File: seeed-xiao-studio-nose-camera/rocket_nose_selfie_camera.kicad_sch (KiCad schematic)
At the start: 20 parts, among them J1 LOGGER TRIGGER / STATUS, J2 UART DEBUG (3V3 TTL), J3 LOGGER CAN, U1 Seeed Studio XIAO ESP32-S3 Se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, U2 SN65HVD230DR

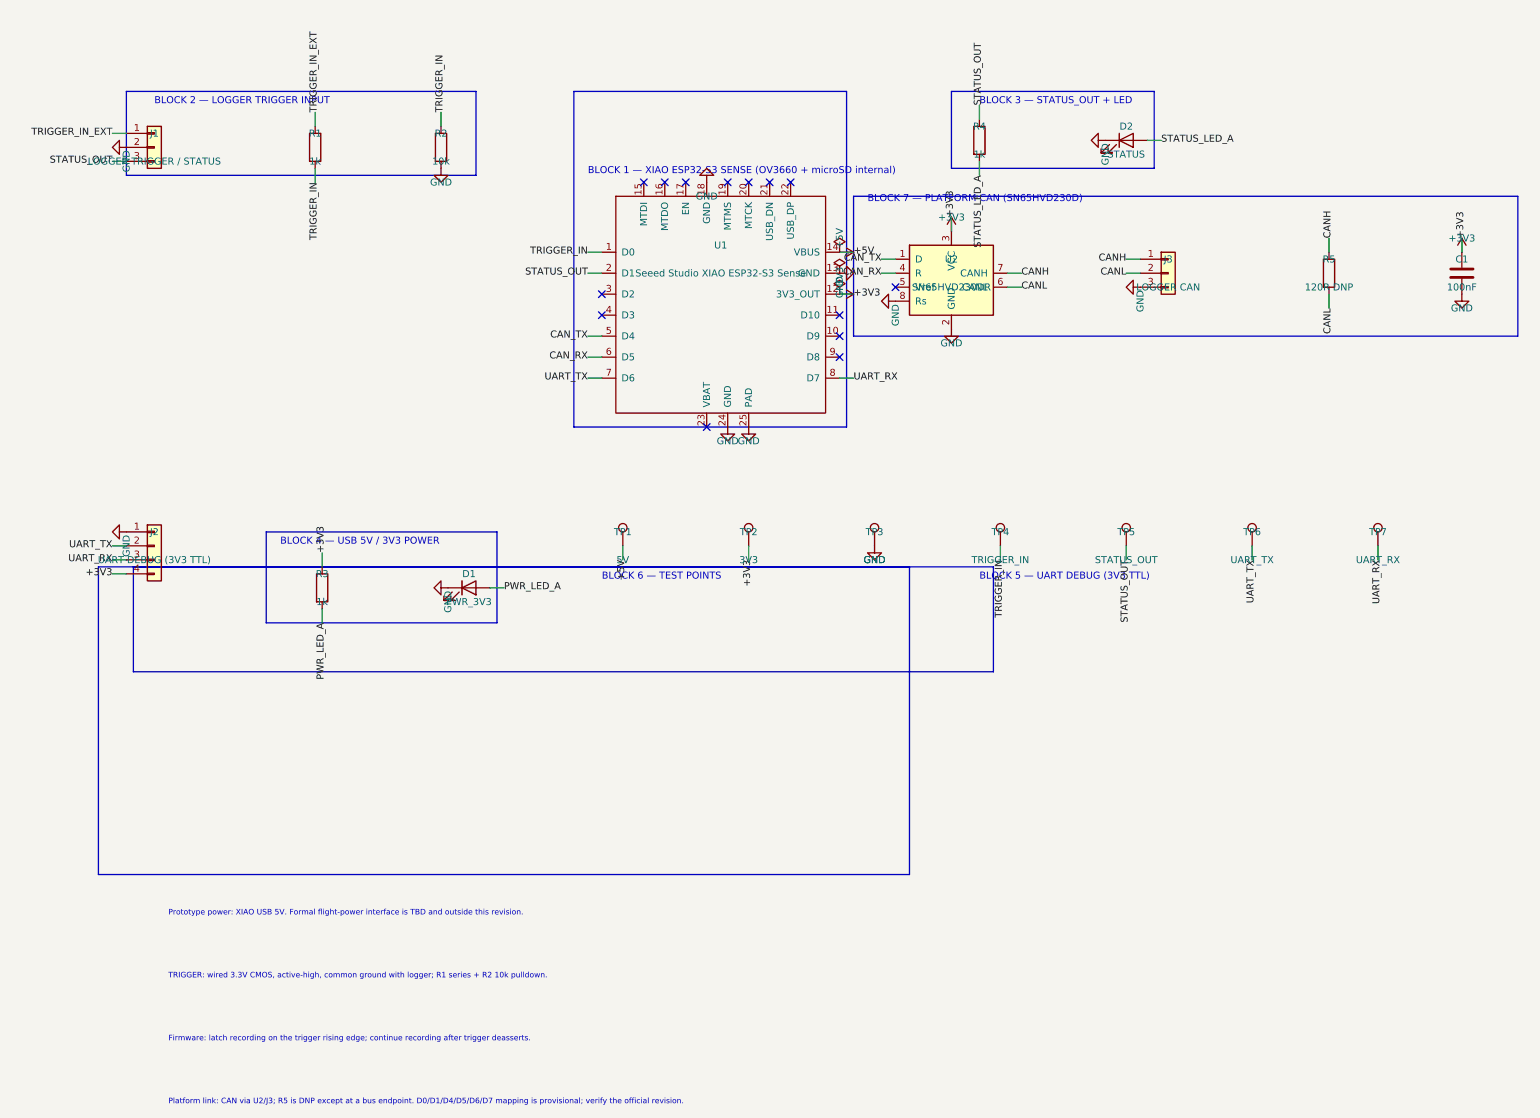
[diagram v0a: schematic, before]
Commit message: sch: logger CAN via MCP2562, separate 5V power input
- Single CAN connector J3 (CANH/CANL/GND) to the logger board; R5 120R fitted as bus endpoint
- J4 becomes a 2-pin +5V/GND input from the power board; D3 B5819W into XIAO VBUS
- Replace SN65HVD230 with MCP2562-E/SN: VDD from 5V_IN (before D3), VIO 3.3V with C2, STBY to GND
- Sync README and BOM with the schematic
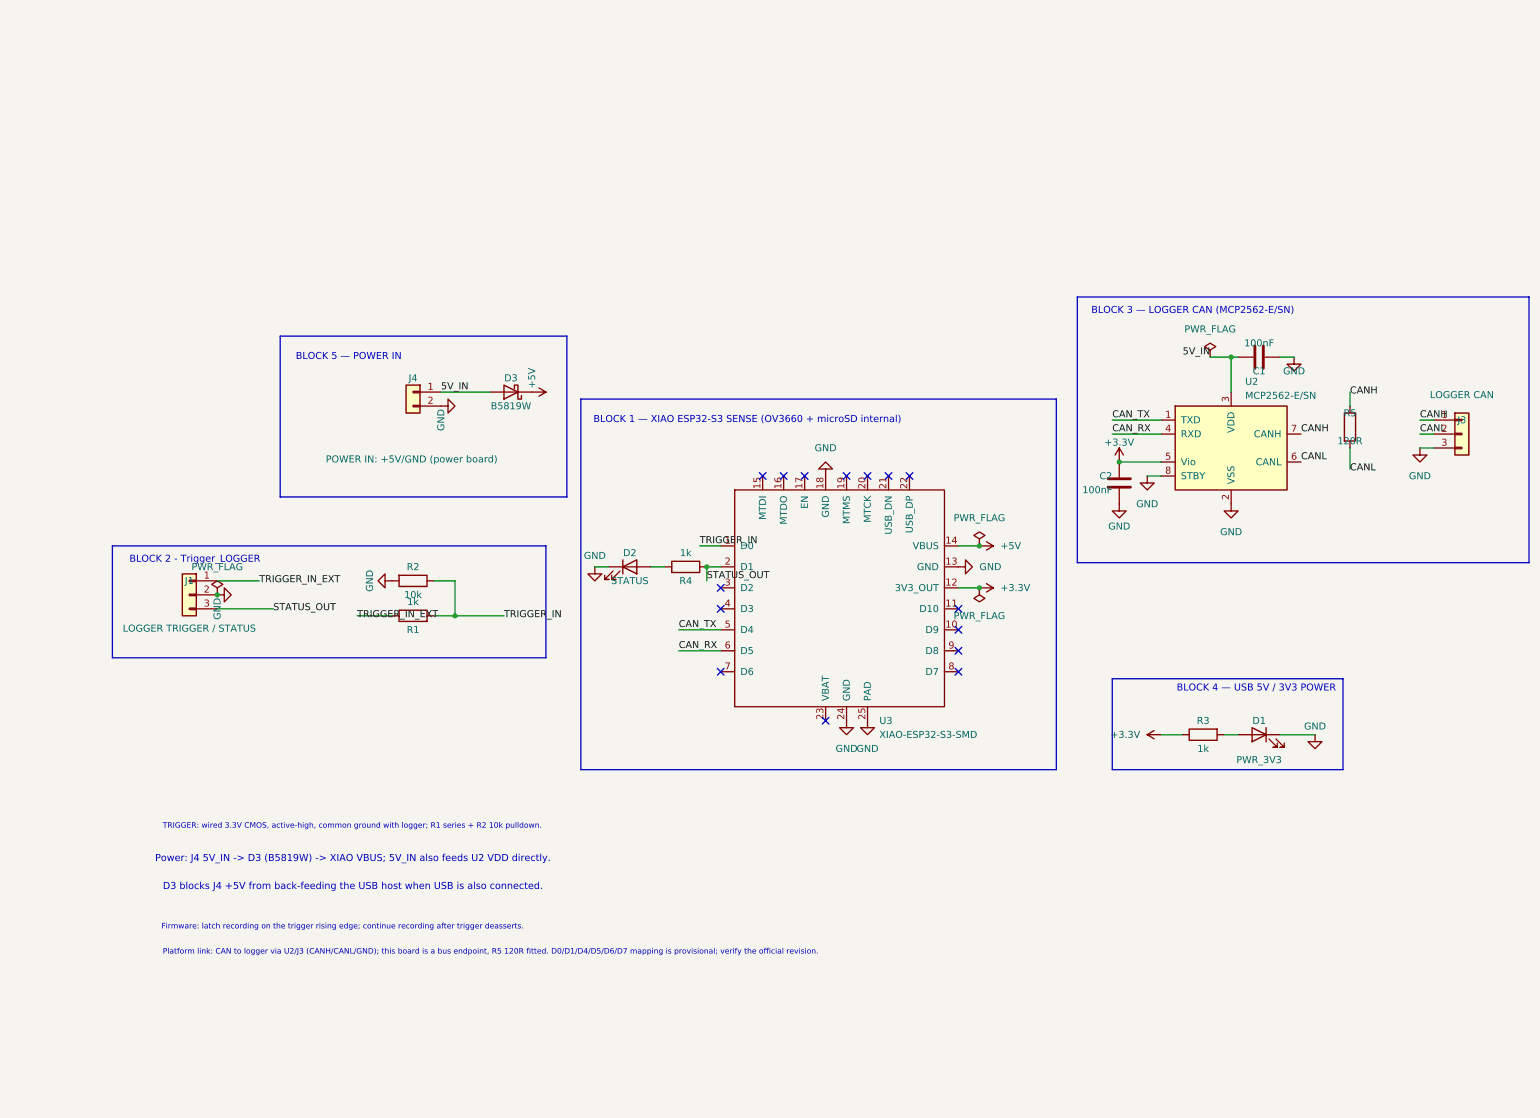
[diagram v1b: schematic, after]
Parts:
- removed J2: UART DEBUG (3V3 TTL), Connector_PinHeader_2.54mm:PinHeader_1x04_P2.54mm_Vertical, symbol Connector_Generic:Conn_01x04
- removed TP1: 5V, TestPoint:TestPoint_Pad_D1.0mm, symbol Connector:TestPoint
- removed TP2: 3V3, TestPoint:TestPoint_Pad_D1.0mm, symbol Connector:TestPoint
- removed TP3: GND, TestPoint:TestPoint_Pad_D1.0mm, symbol Connector:TestPoint
- removed TP4: TRIGGER_IN, TestPoint:TestPoint_Pad_D1.0mm, symbol Connector:TestPoint
- removed TP5: STATUS_OUT, TestPoint:TestPoint_Pad_D1.0mm, symbol Connector:TestPoint
- removed TP6: UART_TX, TestPoint:TestPoint_Pad_D1.0mm, symbol Connector:TestPoint
- removed TP7: UART_RX, TestPoint:TestPoint_Pad_D1.0mm, symbol Connector:TestPoint
- removed U1: Seeed Studio XIAO ESP32-S3 Sense, Seeed_Studio_XIAO_Series:XIAO-ESP32-S3-SMD, symbol Seeed_Studio_XIAO_Series:XIAO-ESP32-S3-SMD
- added C2: 100nF, Capacitor_SMD:C_0603_1608Metric, symbol Device:C
- added D3: B5819W, Diode_SMD:D_SOD-123, symbol Device:D_Schottky
- added J4: POWER IN: +5V/GND (power board), Connector_PinHeader_2.54mm:PinHeader_1x02_P2.54mm_Vertical, symbol Connector_Generic:Conn_01x02
- added U3: XIAO-ESP32-S3-SMD, Seeed_Studio_XIAO_Series:XIAO-ESP32-S3-SMD, symbol Seeed_Studio_XIAO_Series:XIAO-ESP32-S3-SMD
- R5: value 120R DNP -> 120R
- U2: value SN65HVD230DR -> MCP2562-E/SN; symbol Interface_CAN_LIN:SN65HVD230 -> Interface_CAN_LIN:MCP2562-E-SN; MPN SN65HVD230DR -> MCP2562-E/SN
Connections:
- net +5V: now also D3.1 (K), U3.14 (VBUS)
- net CAN_RX: now also U3.6 (D5)
- net CAN_TX: now also U3.5 (D4)
- net GND: now also C1.1, C2.2, J4.2 (Pin_2), U3.13 (GND), U3.18 (GND), U3.24 (GND), U3.25 (PAD); no longer C1.2
- net STATUS_OUT: now also U3.2 (D1)
- net TRIGGER_IN: now also U3.1 (D0)
- net +3.3V: now reaches U2.5 (Vio)
- net +3.3V: now also R3.1, C2.1, U3.12 (3V3_OUT)
- removed net +3V3: C1.1, R3.1, U2.3 (VCC)
- net PWR_LED_A: no longer names the net of D1.2 (A), R3.2
- net STATUS_LED_A: no longer names the net of D2.2 (A), R4.2
- new net 5V_IN: C1.2, D3.2 (A), J4.1 (Pin_1), U2.3 (VDD)
- no-connect marks 14 -> 15
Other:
- note added: "BLOCK 2 - Trigger_LOGGER"
- note added: "BLOCK 3 — LOGGER CAN (MCP2562-E/SN)"
- note added: "BLOCK 5 — POWER IN"
- note added: "D3 blocks J4 +5V from back-feeding the USB host when USB is also connected."
- note added: "Platform link: CAN to logger via U2/J3 (CANH/CANL/GND); this board is a bus endpoint, R5 120R fitted. D0/D1/D4/D5/D6/D7 mapping is provisional; verify the official revision."
- note added: "Power: J4 5V_IN -> D3 (B5819W) -> XIAO VBUS; 5V_IN also feeds U2 VDD directly."
- note removed: "BLOCK 2 — LOGGER TRIGGER INPUT"
- note removed: "BLOCK 3 — STATUS_OUT + LED"
- note removed: "BLOCK 5 — UART DEBUG (3V3 TTL)"
- note removed: "BLOCK 6 — TEST POINTS"
- note removed: "BLOCK 7 — PLATFORM CAN (SN65HVD230D)"
- note removed: "Platform link: CAN via U2/J3; R5 is DNP except at a bus endpoint. D0/D1/D4/D5/D6/D7 mapping is provisional; verify the official revision."
- note removed: "Prototype power: XIAO USB 5V. Formal flight-power interface is TBD and outside this revision."
- moved on the sheet: C1, D1, D2, J1, J3, R1, R2, R3, R4, R5, U2
